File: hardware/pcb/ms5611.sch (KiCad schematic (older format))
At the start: 2 parts, among them U2 ms5611

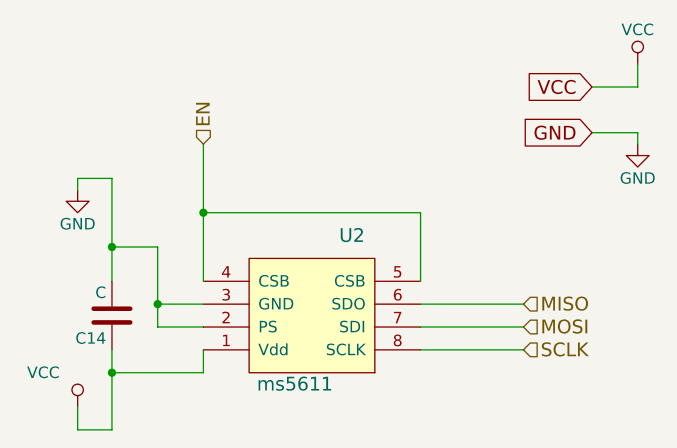
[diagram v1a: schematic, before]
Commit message: Removed nRF8001 connections; beginning eventual design
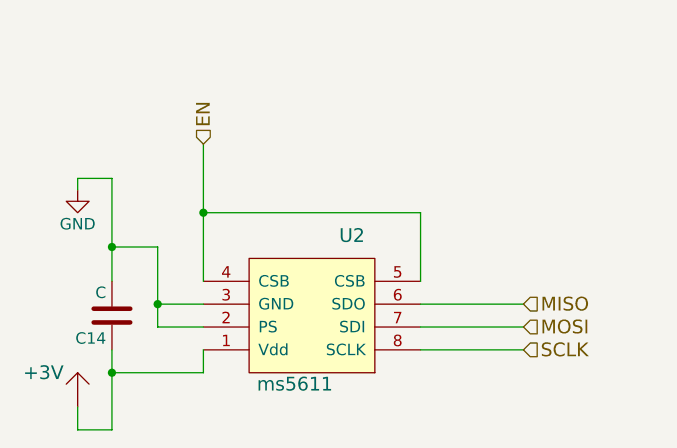
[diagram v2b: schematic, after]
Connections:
- net VCC renamed +3V3
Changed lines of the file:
@@
 	1    0    0    -1
 $EndComp
-$Comp
-L VCC #PWR019
-U 1 1 551EEF4B
-P 4350 4100
-F 0 "#PWR019" H 4350 3950 50  0001 C CNN
-F 1 "VCC" H 4200 4250 50  0000 C CNN
-F 2 "" H 4350 4100 60  0000 C CNN
-F 3 "" H 4350 4100 60  0000 C CNN
-	1    4350 4100
-	1    0    0    -1
-$EndComp
-Text GLabel 6600 2700 0    60   Input ~ 0
-VCC
-Text GLabel 6600 2900 0    60   Input ~ 0
-GND
-$Comp
-L VCC #PWR020
-U 1 1 551F14C2
-P 6800 2600
-F 0 "#PWR020" H 6800 2450 50  0001 C CNN
-F 1 "VCC" H 6800 2750 50  0000 C CNN
-F 2 "" H 6800 2600 60  0000 C CNN
-F 3 "" H 6800 2600 60  0000 C CNN
-	1    6800 2600
-	1    0    0    -1
-$EndComp
-$Comp
-L GND #PWR021
-U 1 1 551F14DA
-P 6800 2950
-F 0 "#PWR021" H 6800 2700 50  0001 C CNN
-F 1 "GND" H 6800 2800 50  0000 C CNN
-F 2 "" H 6800 2950 60  0000 C CNN
-F 3 "" H 6800 2950 60  0000 C CNN
-	1    6800 2950
-	1    0    0    -1
-$EndComp
-Wire Wire Line
-	6600 2900 6800 2900
-Wire Wire Line
-	6800 2900 6800 2950
-Wire Wire Line
-	6800 2600 6800 2700
-Wire Wire Line
-	6800 2700 6600 2700
 Wire Wire Line
 	4500 3100 4500 3550
@@
 	5850 3250 4900 3250
 Connection ~ 4900 3250
+$Comp
+L +3V #PWR019
+U 1 1 55281F01
+P 4350 4100
+F 0 "#PWR019" H 4350 4000 60  0001 C CNN
+F 1 "+3V" H 4200 4250 60  0000 C CNN
+F 2 "" H 4350 4100 60  0000 C CNN
+F 3 "" H 4350 4100 60  0000 C CNN
+	1    4350 4100
+	1    0    0    -1
+$EndComp
 $EndSCHEMATC
